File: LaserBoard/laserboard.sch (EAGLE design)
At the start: 22 parts, among them Q1 BSS138

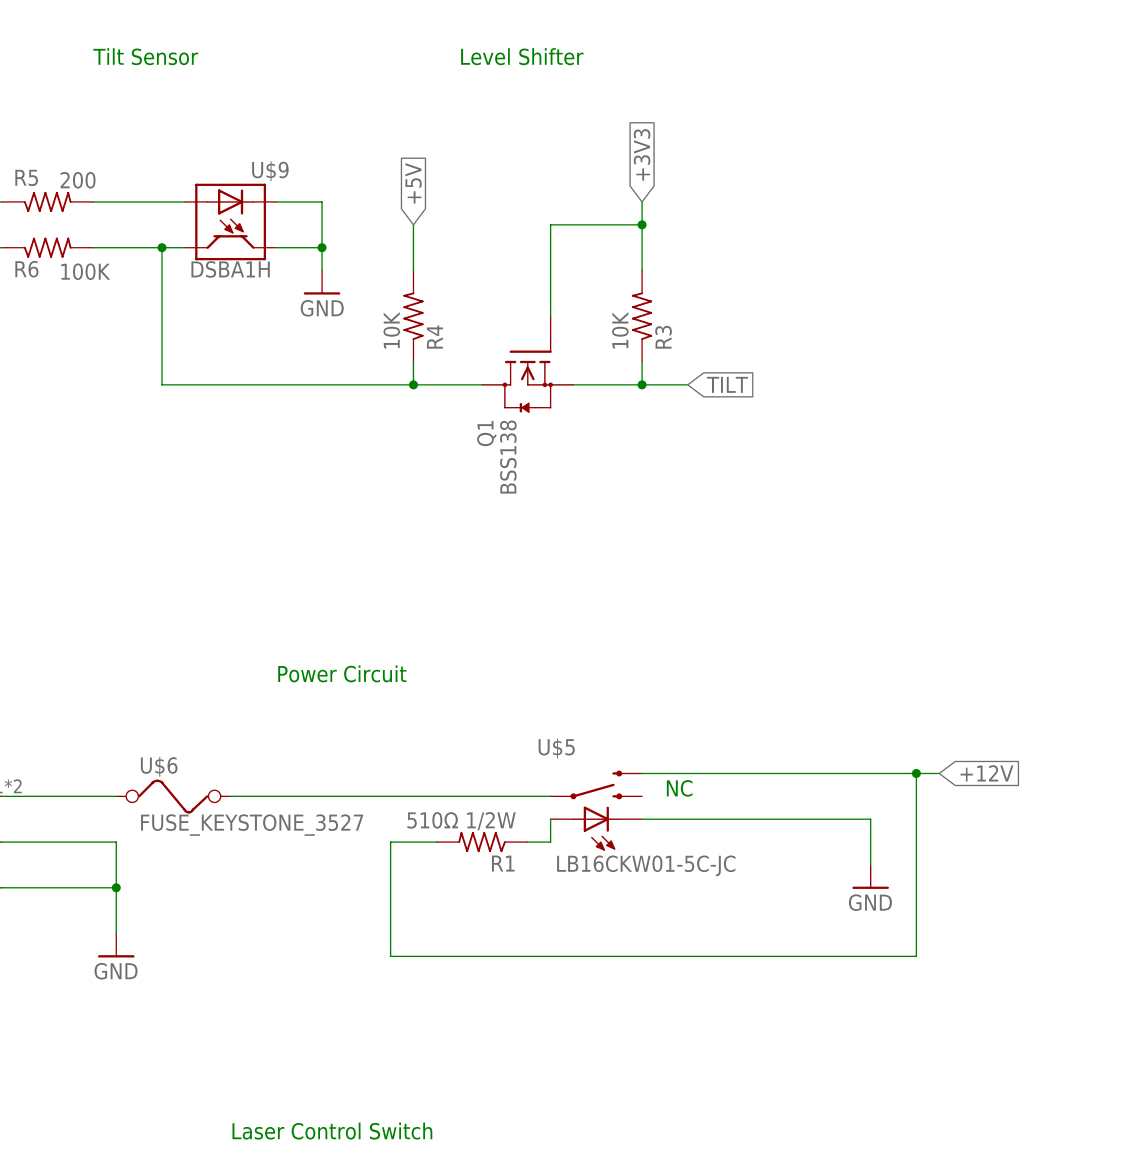
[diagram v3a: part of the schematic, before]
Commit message: Updates to Laser and Power Board
Updated emergency shutoff button footprint, led button voltage changed
to 5v, and switched level shifter to 74LVC1T45.
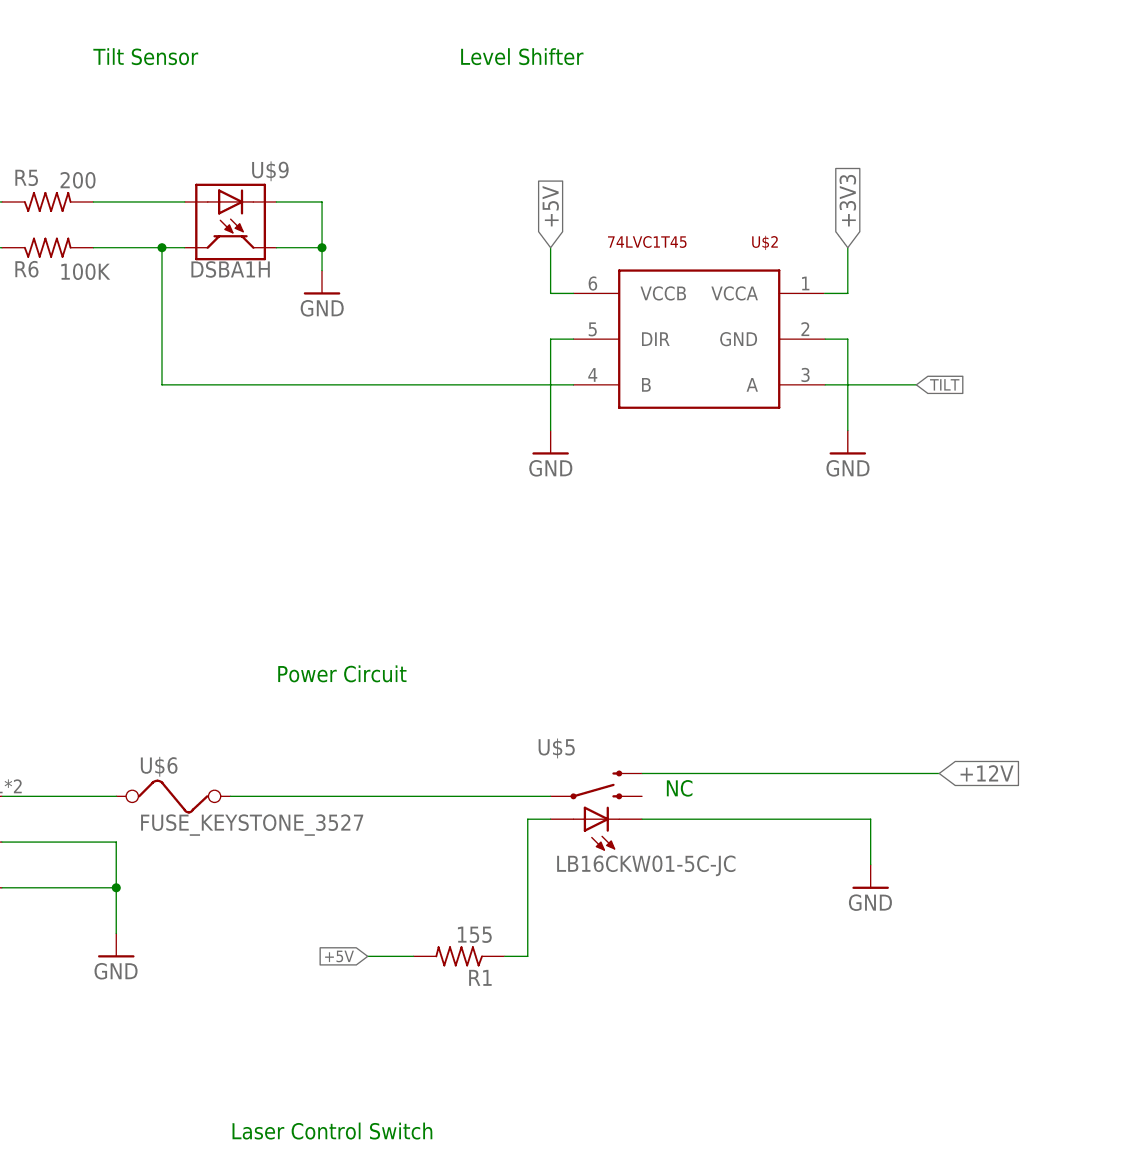
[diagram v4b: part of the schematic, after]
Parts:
- removed Q1: BSS138, m-pad-2.1:BSS138
- removed R3, R4: 10K, rcl:R-US_R0805
- added U$2: 74LVC1T45, ChristiansCustom:74LVC1T45
- R1: value 510Ω 1/2W -> 155
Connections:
- net +12V: no longer R1.2
- net +3V3: now also U$2.VCCA; no longer Q1.G, R3.2
- net +5V: now also R1.2, U$2.VCCB; no longer R4.2
- net GND: now also U$2.DIR, U$2.GND
- net N$5: now also U$2.B; no longer Q1.D, R4.1
- net TILT: now also U$2.A; no longer Q1.S, R3.1
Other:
- moved on the sheet: R1
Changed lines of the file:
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@@
 <part name="U$5" library="ChristiansCustom" deviceset="LB16CKW01-5C-JC" device=""/>
 <part name="GND7" library="supply1" deviceset="GND" device=""/>
-<part name="R1" library="rcl" deviceset="R-US_" device="R0805" value="510Ω 1/2W"/>
+<part name="R1" library="rcl" deviceset="R-US_" device="R0805" value="155"/>
 <part name="U$6" library="ChristiansCustom" deviceset="FUSE_KEYSTONE_3527" device=""/>
 <part name="U$7" library="TPS2023D" deviceset="TPS2023_D_8" device=""/>
@@
 <part name="GND12" library="supply1" deviceset="GND" device=""/>
 <part name="U$8" library="ChristiansCustom" deviceset="CON_2X3_254MM" device=""/>
-<part name="Q1" library="m-pad-2.1" deviceset="BSS138" device=""/>
-<part name="R3" library="rcl" deviceset="R-US_" device="R0805" value="10K"/>
-<part name="R4" library="rcl" deviceset="R-US_" device="R0805" value="10K"/>
 <part name="U$9" library="ChristiansCustom" deviceset="DSBA1H" device=""/>
 <part name="R5" library="rcl" deviceset="R-US_" device="R0805" value="200"/>
 <part name="R6" library="rcl" deviceset="R-US_" device="R0805" value="100K"/>
 <part name="GND13" library="supply1" deviceset="GND" device=""/>
+<part name="U$2" library="ChristiansCustom" deviceset="74LVC1T45" device=""/>
+<part name="GND15" library="supply1" deviceset="GND" device=""/>
+<part name="GND16" library="supply1" deviceset="GND" device=""/>
 </parts>
 <sheets>
@@
 <instance part="U$5" gate="G$1" x="147.32" y="132.08"/>
 <instance part="GND7" gate="1" x="177.8" y="121.92"/>
-<instance part="R1" gate="G$1" x="134.62" y="127" rot="R180"/>
+<instance part="R1" gate="G$1" x="132.08" y="114.3" rot="R180"/>
 <instance part="U$6" gate="G$1" x="101.6" y="132.08"/>
 <instance part="U$7" gate="A" x="93.98" y="73.66"/>
@@
 <instance part="GND12" gate="1" x="215.9" y="198.12"/>
 <instance part="U$8" gate="G$1" x="238.76" y="193.04"/>
-<instance part="Q1" gate="G$1" x="139.7" y="180.34" rot="MR270"/>
-<instance part="R3" gate="G$1" x="152.4" y="185.42" rot="MR90"/>
-<instance part="R4" gate="G$1" x="127" y="185.42" rot="MR90"/>
 <instance part="U$9" gate="G$1" x="106.68" y="195.58" rot="MR0"/>
 <instance part="R5" gate="G$1" x="86.36" y="198.12" smashed="yes" rot="MR180">
@@
 </instance>
 <instance part="GND13" gate="1" x="116.84" y="187.96" rot="MR0"/>
+<instance part="U$2" gate="G$1" x="147.32" y="172.72" rot="MR0"/>
+<instance part="GND15" gate="1" x="175.26" y="170.18" rot="MR0"/>
+<instance part="GND16" gate="1" x="142.24" y="170.18" rot="MR0"/>
 </instances>
 <busses>
@@
 <wire x1="111.76" y1="193.04" x2="116.84" y2="193.04" width="0.1524" layer="91"/>
 <junction x="116.84" y="193.04"/>
+</segment>
+<segment>
+<pinref part="GND16" gate="1" pin="GND"/>
+<wire x1="142.24" y1="172.72" x2="142.24" y2="182.88" width="0.1524" layer="91"/>
+<pinref part="U$2" gate="G$1" pin="DIR"/>
+<wire x1="142.24" y1="182.88" x2="144.78" y2="182.88" width="0.1524" layer="91"/>
+</segment>
+<segment>
+<pinref part="U$2" gate="G$1" pin="GND"/>
+<pinref part="GND15" gate="1" pin="GND"/>
+<wire x1="172.72" y1="182.88" x2="175.26" y2="182.88" width="0.1524" layer="91"/>
+<wire x1="175.26" y1="182.88" x2="175.26" y2="172.72" width="0.1524" layer="91"/>
 </segment>
 </net>
@@
 </segment>
 <segment>
-<pinref part="Q1" gate="G$1" pin="G"/>
-<wire x1="142.24" y1="185.42" x2="142.24" y2="195.58" width="0.1524" layer="91"/>
-<wire x1="142.24" y1="195.58" x2="152.4" y2="195.58" width="0.1524" layer="91"/>
-<pinref part="R3" gate="G$1" pin="2"/>
-<wire x1="152.4" y1="195.58" x2="152.4" y2="190.5" width="0.1524" layer="91"/>
-<wire x1="152.4" y1="195.58" x2="152.4" y2="198.12" width="0.1524" layer="91"/>
-<junction x="152.4" y="195.58"/>
-<label x="152.4" y="198.12" size="1.778" layer="95" rot="MR90" xref="yes"/>
+<wire x1="175.26" y1="193.04" x2="175.26" y2="187.96" width="0.1524" layer="91"/>
+<label x="175.26" y="193.04" size="1.778" layer="95" rot="MR90" xref="yes"/>
+<pinref part="U$2" gate="G$1" pin="VCCA"/>
+<wire x1="172.72" y1="187.96" x2="175.26" y2="187.96" width="0.1524" layer="91"/>
 </segment>
 </net>
@@
 </segment>
 <segment>
-<pinref part="R4" gate="G$1" pin="2"/>
-<wire x1="127" y1="190.5" x2="127" y2="195.58" width="0.1524" layer="91"/>
-<label x="127" y="195.58" size="1.778" layer="95" rot="MR90" xref="yes"/>
+<wire x1="142.24" y1="187.96" x2="142.24" y2="193.04" width="0.1524" layer="91"/>
+<label x="142.24" y="193.04" size="1.778" layer="95" rot="MR90" xref="yes"/>
+<pinref part="U$2" gate="G$1" pin="VCCB"/>
+<wire x1="144.78" y1="187.96" x2="142.24" y2="187.96" width="0.1524" layer="91"/>
 </segment>
 <segment>
@@
 <label x="76.2" y="203.2" size="1.778" layer="95" rot="MR90" xref="yes"/>
 </segment>
+<segment>
+<pinref part="R1" gate="G$1" pin="2"/>
+<wire x1="127" y1="114.3" x2="121.92" y2="114.3" width="0.1524" layer="91"/>
+<label x="121.92" y="114.3" size="1.27" layer="95" rot="R180" xref="yes"/>
+</segment>
 </net>
 <net name="+12V" class="0">
@@
 <segment>
 <pinref part="U$5" gate="G$1" pin="2"/>
-<wire x1="152.4" y1="134.62" x2="182.88" y2="134.62" width="0.1524" layer="91"/>
+<wire x1="152.4" y1="134.62" x2="185.42" y2="134.62" width="0.1524" layer="91"/>
 <label x="185.42" y="134.62" size="1.778" layer="95" xref="yes"/>
-<pinref part="R1" gate="G$1" pin="2"/>
-<wire x1="182.88" y1="134.62" x2="185.42" y2="134.62" width="0.1524" layer="91"/>
-<wire x1="129.54" y1="127" x2="124.46" y2="127" width="0.1524" layer="91"/>
-<wire x1="124.46" y1="127" x2="124.46" y2="114.3" width="0.1524" layer="91"/>
-<wire x1="124.46" y1="114.3" x2="182.88" y2="114.3" width="0.1524" layer="91"/>
-<wire x1="182.88" y1="114.3" x2="182.88" y2="134.62" width="0.1524" layer="91"/>
-<junction x="182.88" y="134.62"/>
 </segment>
 <segment>
@@
 <label x="248.92" y="195.58" size="1.778" layer="95" xref="yes"/>
 <pinref part="U$8" gate="G$1" pin="2"/>
-</segment>
-</net>
-<net name="N$1" class="0">
-<segment>
-<pinref part="R1" gate="G$1" pin="1"/>
-<pinref part="U$5" gate="G$1" pin="+"/>
-<wire x1="139.7" y1="127" x2="142.24" y2="127" width="0.1524" layer="91"/>
-<wire x1="142.24" y1="127" x2="142.24" y2="129.54" width="0.1524" layer="91"/>
 </segment>
 </net>
@@
 </segment>
 <segment>
-<pinref part="R3" gate="G$1" pin="1"/>
-<wire x1="152.4" y1="180.34" x2="152.4" y2="177.8" width="0.1524" layer="91"/>
-<pinref part="Q1" gate="G$1" pin="S"/>
-<wire x1="152.4" y1="177.8" x2="144.78" y2="177.8" width="0.1524" layer="91"/>
-<wire x1="152.4" y1="177.8" x2="157.48" y2="177.8" width="0.1524" layer="91"/>
-<junction x="152.4" y="177.8"/>
-<label x="157.48" y="177.8" size="1.778" layer="95" xref="yes"/>
+<pinref part="U$2" gate="G$1" pin="A"/>
+<wire x1="172.72" y1="177.8" x2="182.88" y2="177.8" width="0.1524" layer="91"/>
+<label x="182.88" y="177.8" size="1.27" layer="95" xref="yes"/>
 </segment>
 </net>
 <net name="N$5" class="0">
 <segment>
-<pinref part="Q1" gate="G$1" pin="D"/>
-<pinref part="R4" gate="G$1" pin="1"/>
-<wire x1="134.62" y1="177.8" x2="127" y2="177.8" width="0.1524" layer="91"/>
-<wire x1="127" y1="177.8" x2="127" y2="180.34" width="0.1524" layer="91"/>
 <pinref part="U$9" gate="G$1" pin="C"/>
 <pinref part="R6" gate="G$1" pin="2"/>
 <wire x1="101.6" y1="193.04" x2="99.06" y2="193.04" width="0.1524" layer="91"/>
 <wire x1="99.06" y1="193.04" x2="91.44" y2="193.04" width="0.1524" layer="91"/>
-<wire x1="127" y1="177.8" x2="99.06" y2="177.8" width="0.1524" layer="91"/>
 <wire x1="99.06" y1="177.8" x2="99.06" y2="193.04" width="0.1524" layer="91"/>
-<junction x="127" y="177.8"/>
 <junction x="99.06" y="193.04"/>
+<wire x1="99.06" y1="177.8" x2="144.78" y2="177.8" width="0.1524" layer="91"/>
+<pinref part="U$2" gate="G$1" pin="B"/>
 </segment>
 </net>
@@
 </segment>
 </net>
+<net name="N$1" class="0">
+<segment>
+<pinref part="R1" gate="G$1" pin="1"/>
+<wire x1="137.16" y1="114.3" x2="139.7" y2="114.3" width="0.1524" layer="91"/>
+<wire x1="139.7" y1="114.3" x2="139.7" y2="129.54" width="0.1524" layer="91"/>
+<pinref part="U$5" gate="G$1" pin="+"/>
+<wire x1="139.7" y1="129.54" x2="142.24" y2="129.54" width="0.1524" layer="91"/>
+</segment>
+</net>

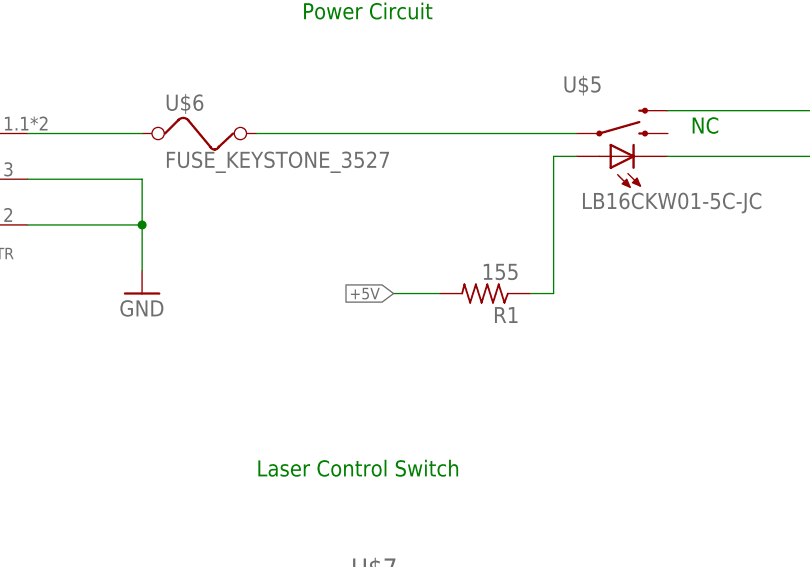
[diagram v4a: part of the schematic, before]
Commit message: Final Revisions to PCBs and Schematics
Final revisions made to the PCBs and schematics. This is the version
which will be sent out to the board house for round two.
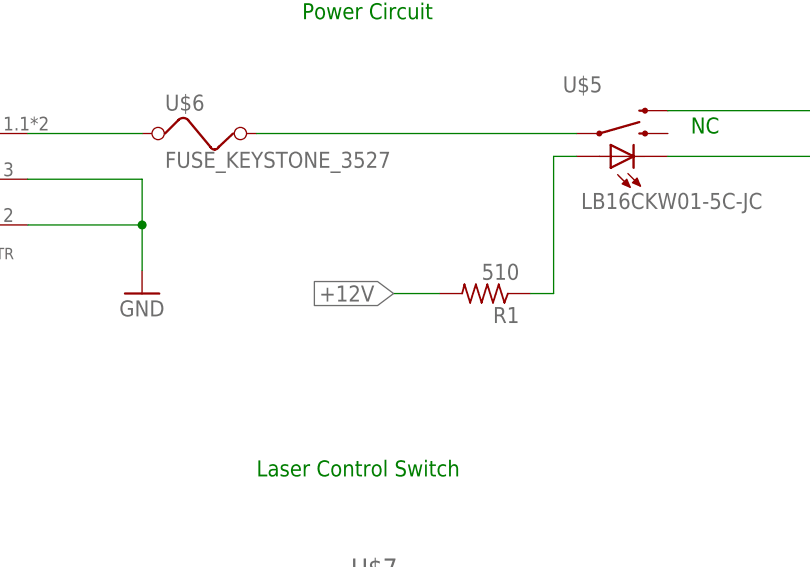
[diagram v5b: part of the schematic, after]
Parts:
- R1: value 155 -> 510
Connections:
- net +12V: now also R1.2
- net +5V: no longer R1.2
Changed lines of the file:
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@@
 <part name="U$5" library="ChristiansCustom" deviceset="LB16CKW01-5C-JC" device=""/>
 <part name="GND7" library="supply1" deviceset="GND" device=""/>
-<part name="R1" library="rcl" deviceset="R-US_" device="R0805" value="155"/>
+<part name="R1" library="rcl" deviceset="R-US_" device="R0805" value="510"/>
 <part name="U$6" library="ChristiansCustom" deviceset="FUSE_KEYSTONE_3527" device=""/>
 <part name="U$7" library="TPS2023D" deviceset="TPS2023_D_8" device=""/>
@@
 <label x="76.2" y="203.2" size="1.778" layer="95" rot="MR90" xref="yes"/>
 </segment>
-<segment>
-<pinref part="R1" gate="G$1" pin="2"/>
-<wire x1="127" y1="114.3" x2="121.92" y2="114.3" width="0.1524" layer="91"/>
-<label x="121.92" y="114.3" size="1.27" layer="95" rot="R180" xref="yes"/>
-</segment>
 </net>
 <net name="+12V" class="0">
@@
 <pinref part="U$8" gate="G$1" pin="2"/>
 </segment>
+<segment>
+<pinref part="R1" gate="G$1" pin="2"/>
+<wire x1="127" y1="114.3" x2="121.92" y2="114.3" width="0.1524" layer="91"/>
+<label x="121.92" y="114.3" size="1.778" layer="95" rot="R180" xref="yes"/>
+</segment>
 </net>
